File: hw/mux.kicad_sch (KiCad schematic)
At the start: 7 parts, among them U11 NCP708, U6 TS3USB3031

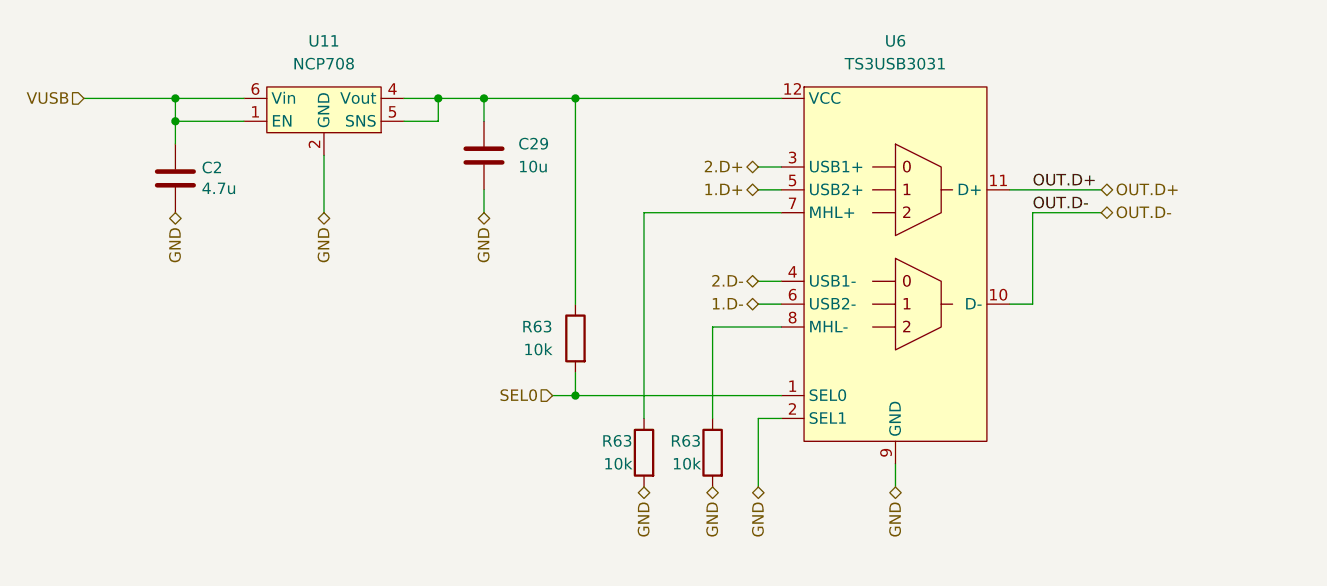
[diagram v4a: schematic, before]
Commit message: Blocking the robot switching on by spinning a motor
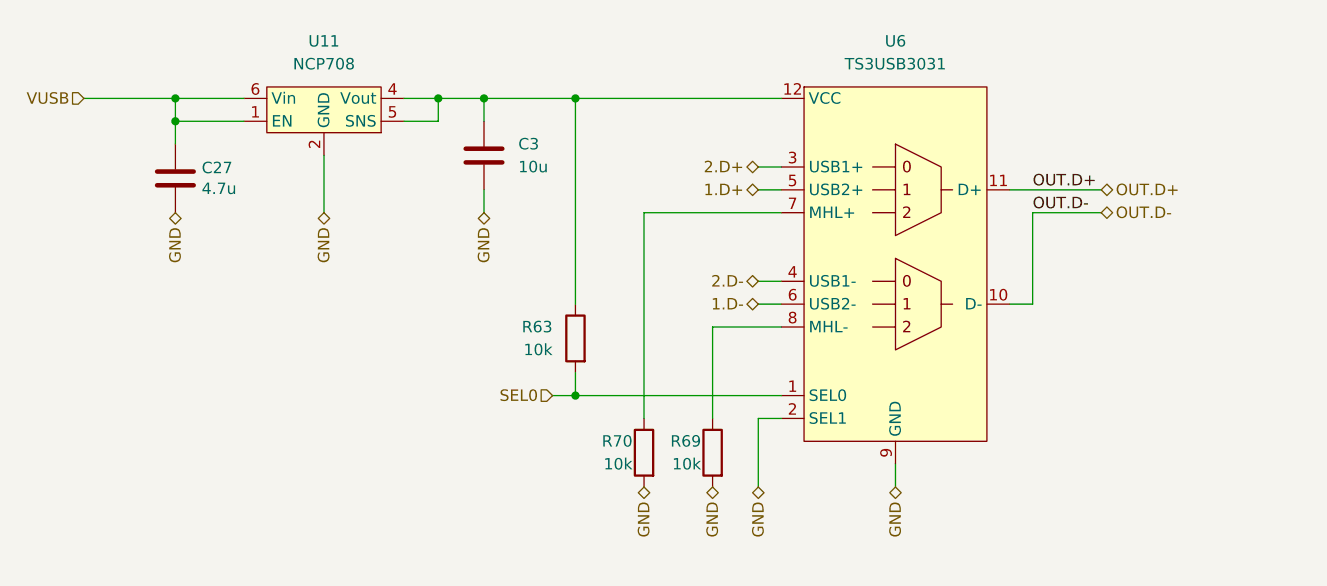
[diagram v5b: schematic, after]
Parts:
- renumbered C2 to C27, C29 to C3, R63 to R69, R63 to R70
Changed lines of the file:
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@@
   (symbol (lib_id "Device:C") (at 100.33 72.39 0) (unit 1)
     (in_bom yes) (on_board yes) (dnp no)
-    (property "Reference" "C2" (at 103.251 71.2216 0)
+    (property "Reference" "C27" (at 103.251 71.2216 0)
       (effects (font (size 1.27 1.27)) (justify left))
     )
@@
     (instances
       (project "Zelvicka"
-        (path "/04d53a73-373f-40ca-9ff1-406e2f105d42/b25751f2-11c3-433a-b099-5c0b39b7078e/d79845a6-d2a4-49ac-97d6-5f5626f716cd"
-          (reference "C2") (unit 1)
-        )
         (path "/04d53a73-373f-40ca-9ff1-406e2f105d42/cf5a8cac-e720-4f6c-b6d8-8f40c3604d15/5f9eb313-4daf-4894-964c-3ee2f806bea1"
           (reference "C27") (unit 1)
@@
   (symbol (lib_id "Device:R") (at 152.4 102.87 0) (mirror y) (unit 1)
     (in_bom yes) (on_board yes) (dnp no)
-    (property "Reference" "R63" (at 151.13 101.6 0)
+    (property "Reference" "R70" (at 151.13 101.6 0)
       (effects (font (size 1.27 1.27)) (justify left))
     )
@@
     (instances
       (project "Zelvicka"
-        (path "/04d53a73-373f-40ca-9ff1-406e2f105d42/b25751f2-11c3-433a-b099-5c0b39b7078e/e22ea24c-0368-422d-a8f9-a65d7c1f87fe"
-          (reference "R63") (unit 1)
-        )
-        (path "/04d53a73-373f-40ca-9ff1-406e2f105d42"
-          (reference "R63") (unit 1)
-        )
         (path "/04d53a73-373f-40ca-9ff1-406e2f105d42/cf5a8cac-e720-4f6c-b6d8-8f40c3604d15/5f9eb313-4daf-4894-964c-3ee2f806bea1"
           (reference "R70") (unit 1)
@@
     (instances
       (project "Zelvicka"
-        (path "/04d53a73-373f-40ca-9ff1-406e2f105d42/b25751f2-11c3-433a-b099-5c0b39b7078e/e22ea24c-0368-422d-a8f9-a65d7c1f87fe"
+        (path "/04d53a73-373f-40ca-9ff1-406e2f105d42/cf5a8cac-e720-4f6c-b6d8-8f40c3604d15/5f9eb313-4daf-4894-964c-3ee2f806bea1"
           (reference "R63") (unit 1)
         )
-        (path "/04d53a73-373f-40ca-9ff1-406e2f105d42"
-          (reference "R63") (unit 1)
-        )
-        (path "/04d53a73-373f-40ca-9ff1-406e2f105d42/cf5a8cac-e720-4f6c-b6d8-8f40c3604d15/5f9eb313-4daf-4894-964c-3ee2f806bea1"
-          (reference "R63") (unit 1)
-        )
       )
     )
@@
   (symbol (lib_id "Device:R") (at 160.02 102.87 0) (mirror y) (unit 1)
     (in_bom yes) (on_board yes) (dnp no)
-    (property "Reference" "R63" (at 158.75 101.6 0)
+    (property "Reference" "R69" (at 158.75 101.6 0)
       (effects (font (size 1.27 1.27)) (justify left))
     )
@@
     (instances
       (project "Zelvicka"
-        (path "/04d53a73-373f-40ca-9ff1-406e2f105d42/b25751f2-11c3-433a-b099-5c0b39b7078e/e22ea24c-0368-422d-a8f9-a65d7c1f87fe"
-          (reference "R63") (unit 1)
-        )
-        (path "/04d53a73-373f-40ca-9ff1-406e2f105d42"
-          (reference "R63") (unit 1)
-        )
         (path "/04d53a73-373f-40ca-9ff1-406e2f105d42/cf5a8cac-e720-4f6c-b6d8-8f40c3604d15/5f9eb313-4daf-4894-964c-3ee2f806bea1"
           (reference "R69") (unit 1)
@@
   (symbol (lib_id "Device:C") (at 134.62 69.85 0) (unit 1)
     (in_bom yes) (on_board yes) (dnp no) (fields_autoplaced)
-    (property "Reference" "C29" (at 138.43 68.5799 0)
+    (property "Reference" "C3" (at 138.43 68.5799 0)
       (effects (font (size 1.27 1.27)) (justify left))
     )
@@
     (instances
       (project "Zelvicka"
-        (path "/04d53a73-373f-40ca-9ff1-406e2f105d42/b25751f2-11c3-433a-b099-5c0b39b7078e/d79845a6-d2a4-49ac-97d6-5f5626f716cd"
-          (reference "C29") (unit 1)
-        )
         (path "/04d53a73-373f-40ca-9ff1-406e2f105d42/cf5a8cac-e720-4f6c-b6d8-8f40c3604d15/5f9eb313-4daf-4894-964c-3ee2f806bea1"
           (reference "C3") (unit 1)

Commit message: Change battery charger
By replacing the charger the price was reduced by about 120kč (5.5$)
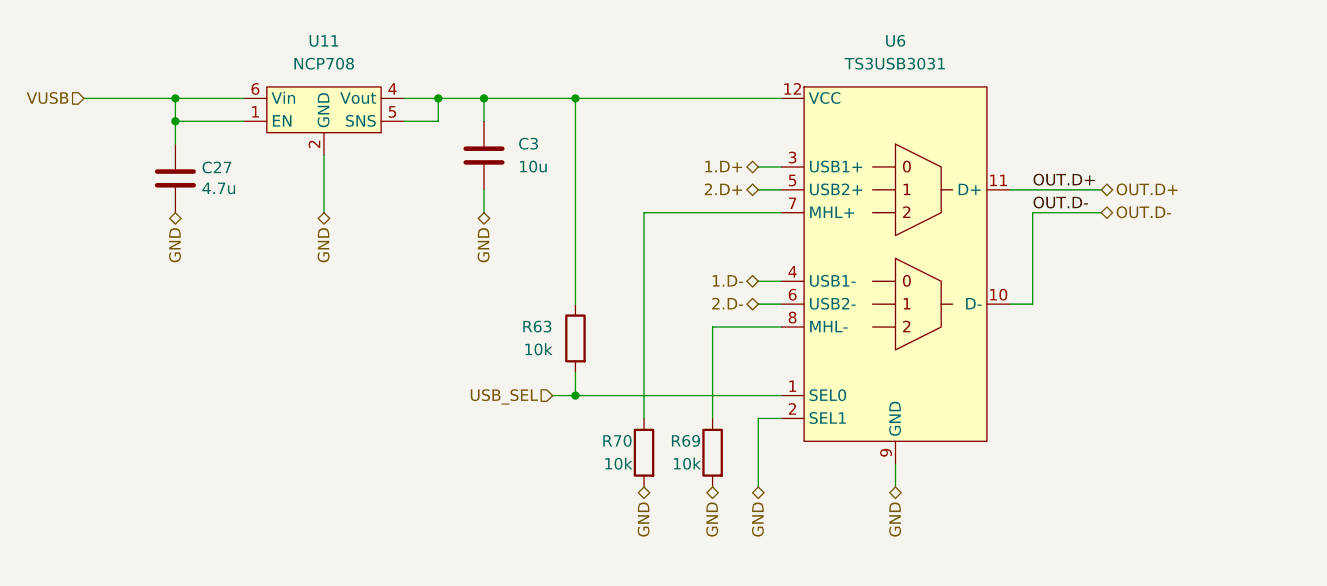
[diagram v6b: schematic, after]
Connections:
- net 1.D+: now also U6.3 (USB1+); no longer U6.5 (USB2+)
- net 1.D-: now also U6.4 (USB1-); no longer U6.6 (USB2-)
- net 2.D+: now also U6.5 (USB2+); no longer U6.3 (USB1+)
- net 2.D-: now also U6.6 (USB2-); no longer U6.4 (USB1-)
- net SEL0 renamed USB_SEL
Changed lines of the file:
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@@
     (effects (font (size 1.27 1.27)) (justify left bottom))
   )
-  (hierarchical_label "2.D-" (shape bidirectional) (at 165.1 83.82 180) (fields_autoplaced)
+  (hierarchical_label "2.D-" (shape bidirectional) (at 165.1 86.36 180) (fields_autoplaced)
     (effects (font (size 1.27 1.27)) (justify right))
   )
@@
     (effects (font (size 1.27 1.27)) (justify right))
   )
-  (hierarchical_label "1.D-" (shape bidirectional) (at 165.1 86.36 180) (fields_autoplaced)
+  (hierarchical_label "1.D-" (shape bidirectional) (at 165.1 83.82 180) (fields_autoplaced)
     (effects (font (size 1.27 1.27)) (justify right))
   )
@@
     (effects (font (size 1.27 1.27)) (justify right))
   )
-  (hierarchical_label "2.D+" (shape bidirectional) (at 165.1 71.12 180) (fields_autoplaced)
+  (hierarchical_label "2.D+" (shape bidirectional) (at 165.1 73.66 180) (fields_autoplaced)
     (effects (font (size 1.27 1.27)) (justify right))
   )
@@
     (effects (font (size 1.27 1.27)) (justify left))
   )
-  (hierarchical_label "1.D+" (shape bidirectional) (at 165.1 73.66 180) (fields_autoplaced)
+  (hierarchical_label "1.D+" (shape bidirectional) (at 165.1 71.12 180) (fields_autoplaced)
     (effects (font (size 1.27 1.27)) (justify right))
   )
@@
     (effects (font (size 1.27 1.27)) (justify right))
   )
-  (hierarchical_label "SEL0" (shape input) (at 142.24 96.52 180) (fields_autoplaced)
+  (hierarchical_label "USB_SEL" (shape input) (at 142.24 96.52 180) (fields_autoplaced)
     (effects (font (size 1.27 1.27)) (justify right))
   )

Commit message: Resolves #75 change line sensor mux and USB mux
Reducing the number of components and their price
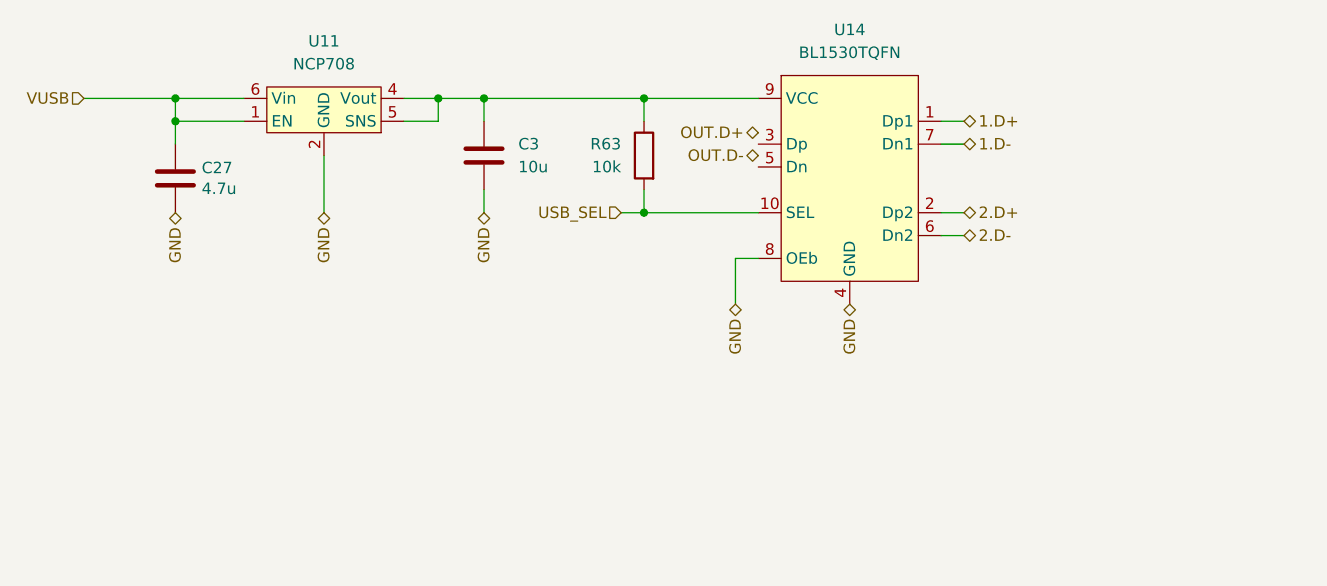
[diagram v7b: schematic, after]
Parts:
- removed R69, R70: 10k, Resistor_SMD:R_0402_1005Metric, symbol Device:R
- removed U6: TS3USB3031, Package_DFN_QFN:Texas_X2QFN-12_1.6x1.6mm_P0.4mm, symbol RKL-DiscreteLogic:TS3USB3031
- added U14: BL1530TQFN, Package_DFN_QFN:UQFN-10_1.4x1.8mm_P0.4mm, symbol RKL-Uncategorized:BL1530TQFN
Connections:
- net 1.D+: now also U14.1 (Dp1)
- net 1.D-: now also U14.7 (Dn1)
- net 2.D+: now also U14.2 (Dp2)
- net 2.D-: now also U14.6 (Dn2)
- net GND: now also U14.4 (GND), U14.8 (OEb)
- net USB_SEL: now also U14.10 (SEL)
- net at C3.1, R63.1, U11.4 (Vout)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: now also U14.9 (VCC)
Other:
- moved on the sheet: R63

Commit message: Mišmaš
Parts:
- removed C27: 4.7u, Capacitor_SMD:C_0603_1608Metric, symbol Device:C
- removed U11: NCP708, RKL-StandardPackages:UDFN6-3x3mm, symbol RKL-LDO:NCP708
- C3: Price (100ks) (none) -> 0.0159; Price (1ks) (none) -> 0.0159
- R63: Price (100ks) (none) -> 0.0005; Price (1ks) (none) -> 0.0005
- U14: Basic/Extended (none) -> E; Price (100ks) (none) -> 0.1148; Price (1ks) (none) -> 0.1445
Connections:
- net OUT.D+: now also U14.3 (Dp)
- net OUT.D-: now also U14.5 (Dn)
- net VUSB: now also C3.1, R63.1, U14.9 (VCC)
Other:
- moved on the sheet: C3, R63, U14
